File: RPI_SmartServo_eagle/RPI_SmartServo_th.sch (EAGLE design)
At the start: 39 parts, among them Q1 MCP9701A-E/TO, U1 ZXCT1009

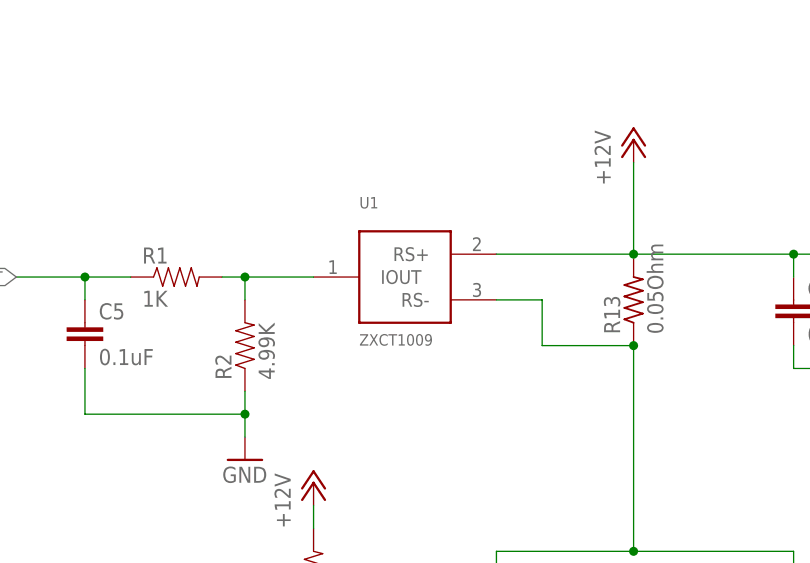
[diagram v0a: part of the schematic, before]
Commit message: Changed the Current Sensor 	modificado: RPI_SmartServo_eagle/RPI_SmartServo_th.brd 	modificado: RPI_SmartServo_eagle/RPI_SmartServo_th.sch
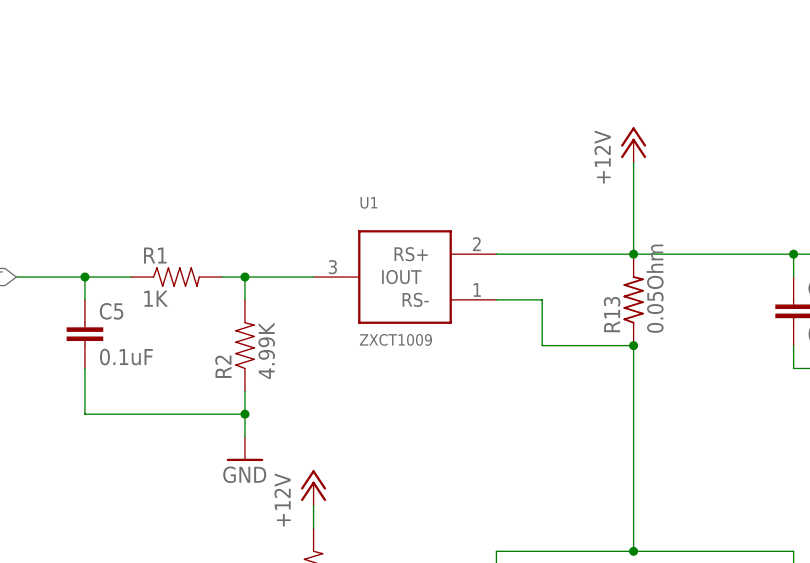
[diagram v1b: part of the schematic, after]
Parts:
- U1: device WSNlib:ZXCT1009 -> 00LibreriaErle:ZXCT1009
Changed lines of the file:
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@@
 <parts>
 <part name="FRAME1" library="SparkFun-Aesthetics" deviceset="FRAME-A4L" device=""/>
-<part name="U1" library="WSNlib" deviceset="ZXCT1009" device=""/>
 <part name="R1" library="SparkFun-Resistors" deviceset="RESISTOR" device="PTH-1/4W" value="1K"/>
 <part name="R2" library="SparkFun-Resistors" deviceset="RESISTOR" device="PTH-1/4W" value="4.99K"/>
@@
 <part name="M-" library="wirepad" deviceset="1,6/0,9" device=""/>
 <part name="GND13" library="SparkFun-Aesthetics" deviceset="GND" device=""/>
+<part name="U1" library="00LibreriaErle" deviceset="ZXCT1009" device=""/>
 </parts>
 <sheets>
@@
 <instances>
 <instance part="FRAME1" gate="G$1" x="0" y="0"/>
-<instance part="U1" gate="G$1" x="185.42" y="142.24" rot="R270"/>
 <instance part="R1" gate="G$1" x="160.02" y="144.78"/>
 <instance part="R2" gate="G$1" x="167.64" y="137.16" rot="R90"/>
@@
 <instance part="M-" gate="1" x="215.9" y="93.98"/>
 <instance part="GND13" gate="1" x="127" y="109.22"/>
+<instance part="U1" gate="G$1" x="185.42" y="142.24" rot="R270"/>
 </instances>
 <busses>
@@
 <segment>
 <pinref part="R1" gate="G$1" pin="2"/>
-<pinref part="U1" gate="G$1" pin="IOUT"/>
 <wire x1="165.1" y1="144.78" x2="167.64" y2="144.78" width="0.1524" layer="91"/>
 <pinref part="R2" gate="G$1" pin="2"/>
@@
 <wire x1="167.64" y1="142.24" x2="167.64" y2="144.78" width="0.1524" layer="91"/>
 <junction x="167.64" y="144.78"/>
+<pinref part="U1" gate="G$1" pin="IOUT"/>
 </segment>
 </net>
@@
 <net name="N$12" class="0">
 <segment>
-<pinref part="U1" gate="G$1" pin="RS-"/>
 <wire x1="195.58" y1="142.24" x2="200.66" y2="142.24" width="0.1524" layer="91"/>
 <wire x1="200.66" y1="142.24" x2="200.66" y2="137.16" width="0.1524" layer="91"/>
@@
 <junction x="210.82" y="137.16"/>
 <junction x="210.82" y="114.3"/>
+<pinref part="U1" gate="G$1" pin="RS-"/>
 </segment>
 </net>
@@
 </segment>
 <segment>
-<pinref part="U1" gate="G$1" pin="RS+"/>
 <pinref part="R13" gate="G$1" pin="2"/>
 <wire x1="195.58" y1="147.32" x2="210.82" y2="147.32" width="0.1524" layer="91"/>
@@
 <junction x="228.6" y="147.32"/>
 <pinref part="P+2" gate="1" pin="+12V"/>
-</segment>
-<segment>
+<pinref part="U1" gate="G$1" pin="RS+"/>
+</segment>
+<segment>
